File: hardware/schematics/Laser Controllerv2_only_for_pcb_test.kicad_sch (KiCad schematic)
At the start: 98 parts, among them J1 SD Card Module (6-pin, 2.54mm), J2 PWR IN VIN_BUCK (10-30V), J3 PWR IN Galvo, J4 FAN1 PWR IN, J5 FAN1, J6 FAN2 PWR IN, J7 FAN2, U1 ESP32-S3-N16R8-DevKit, U10 DS18B20, U12 OPA4134UA_2K5, U13 Galvo Input, U15 6N137, U16 6N137, U17 6N137, U2 DAC8562SDGST, U3 TTL_RGB Blue, U4 TTL_RGB Red, U5 TTL_RGB Green, U6 DS18B20, U7 DS18B20, U8 DS18B20, U9 DS18B20

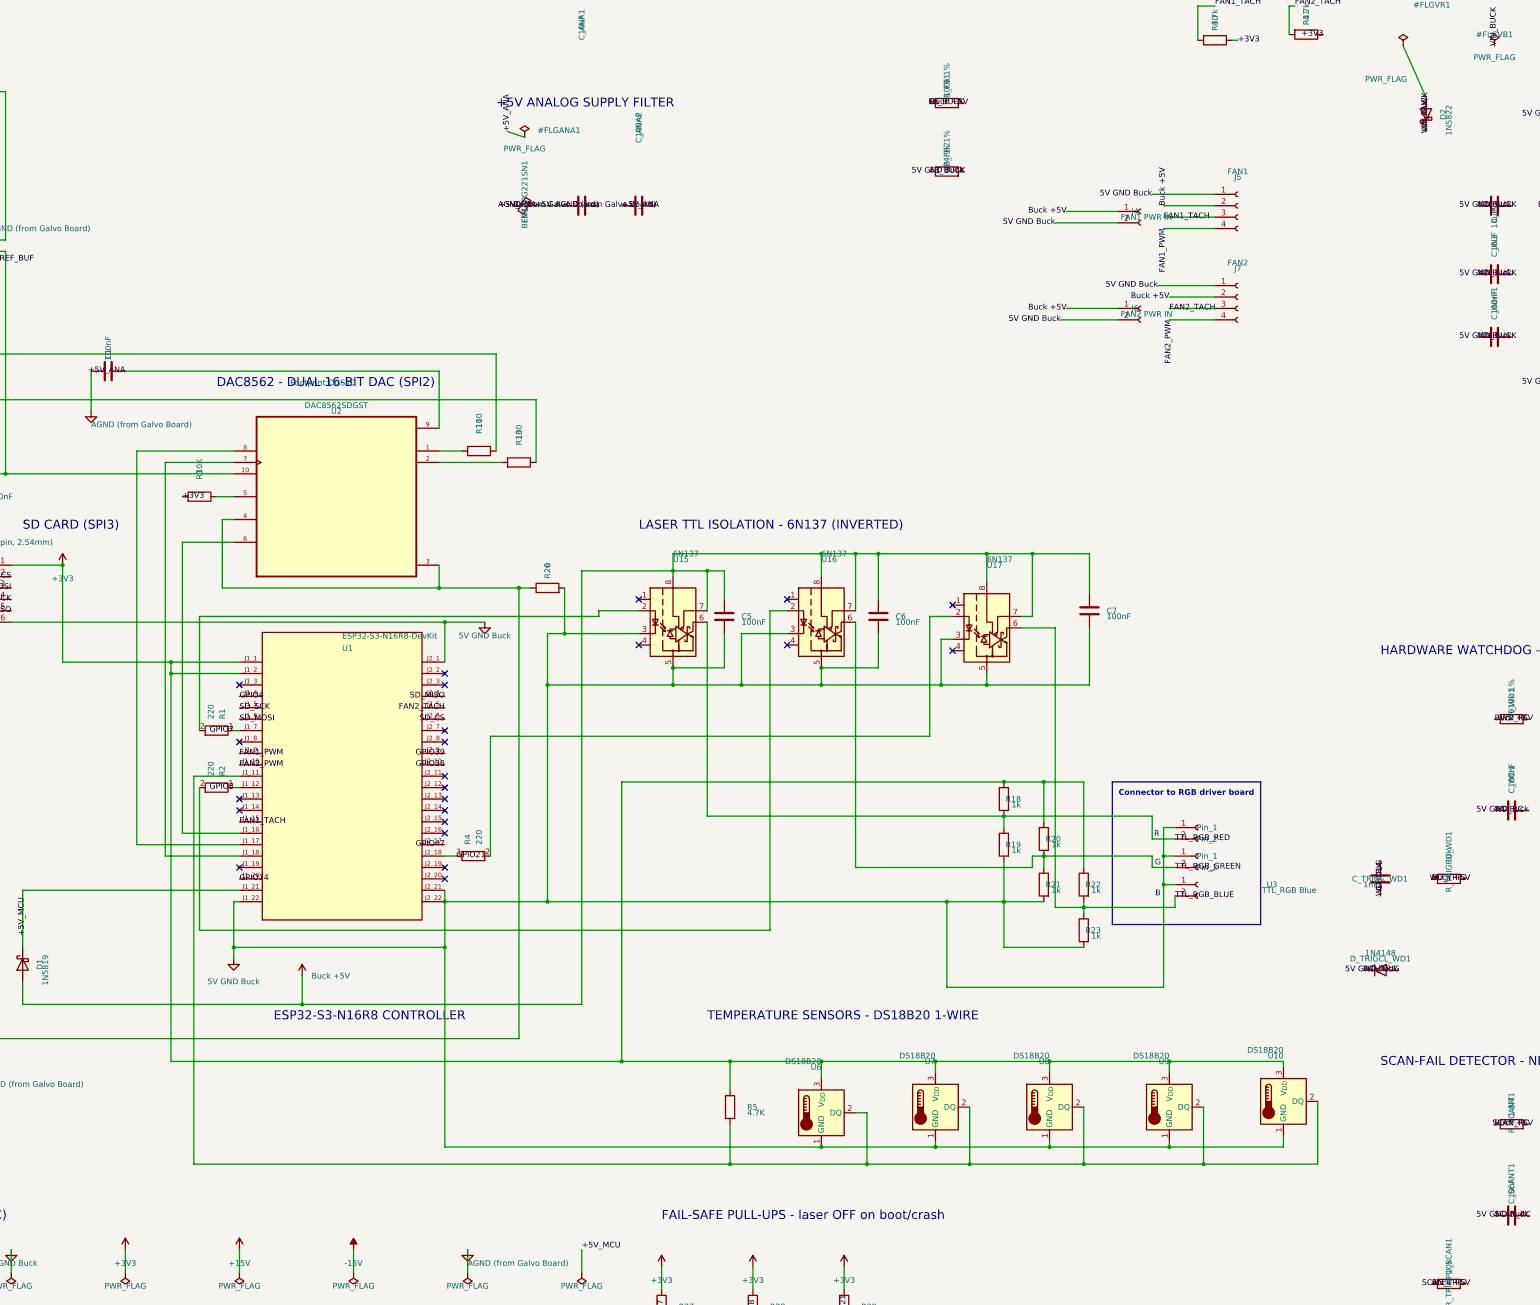
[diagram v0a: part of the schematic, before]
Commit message: hw: make v2 schematic portable and add supply decoupling
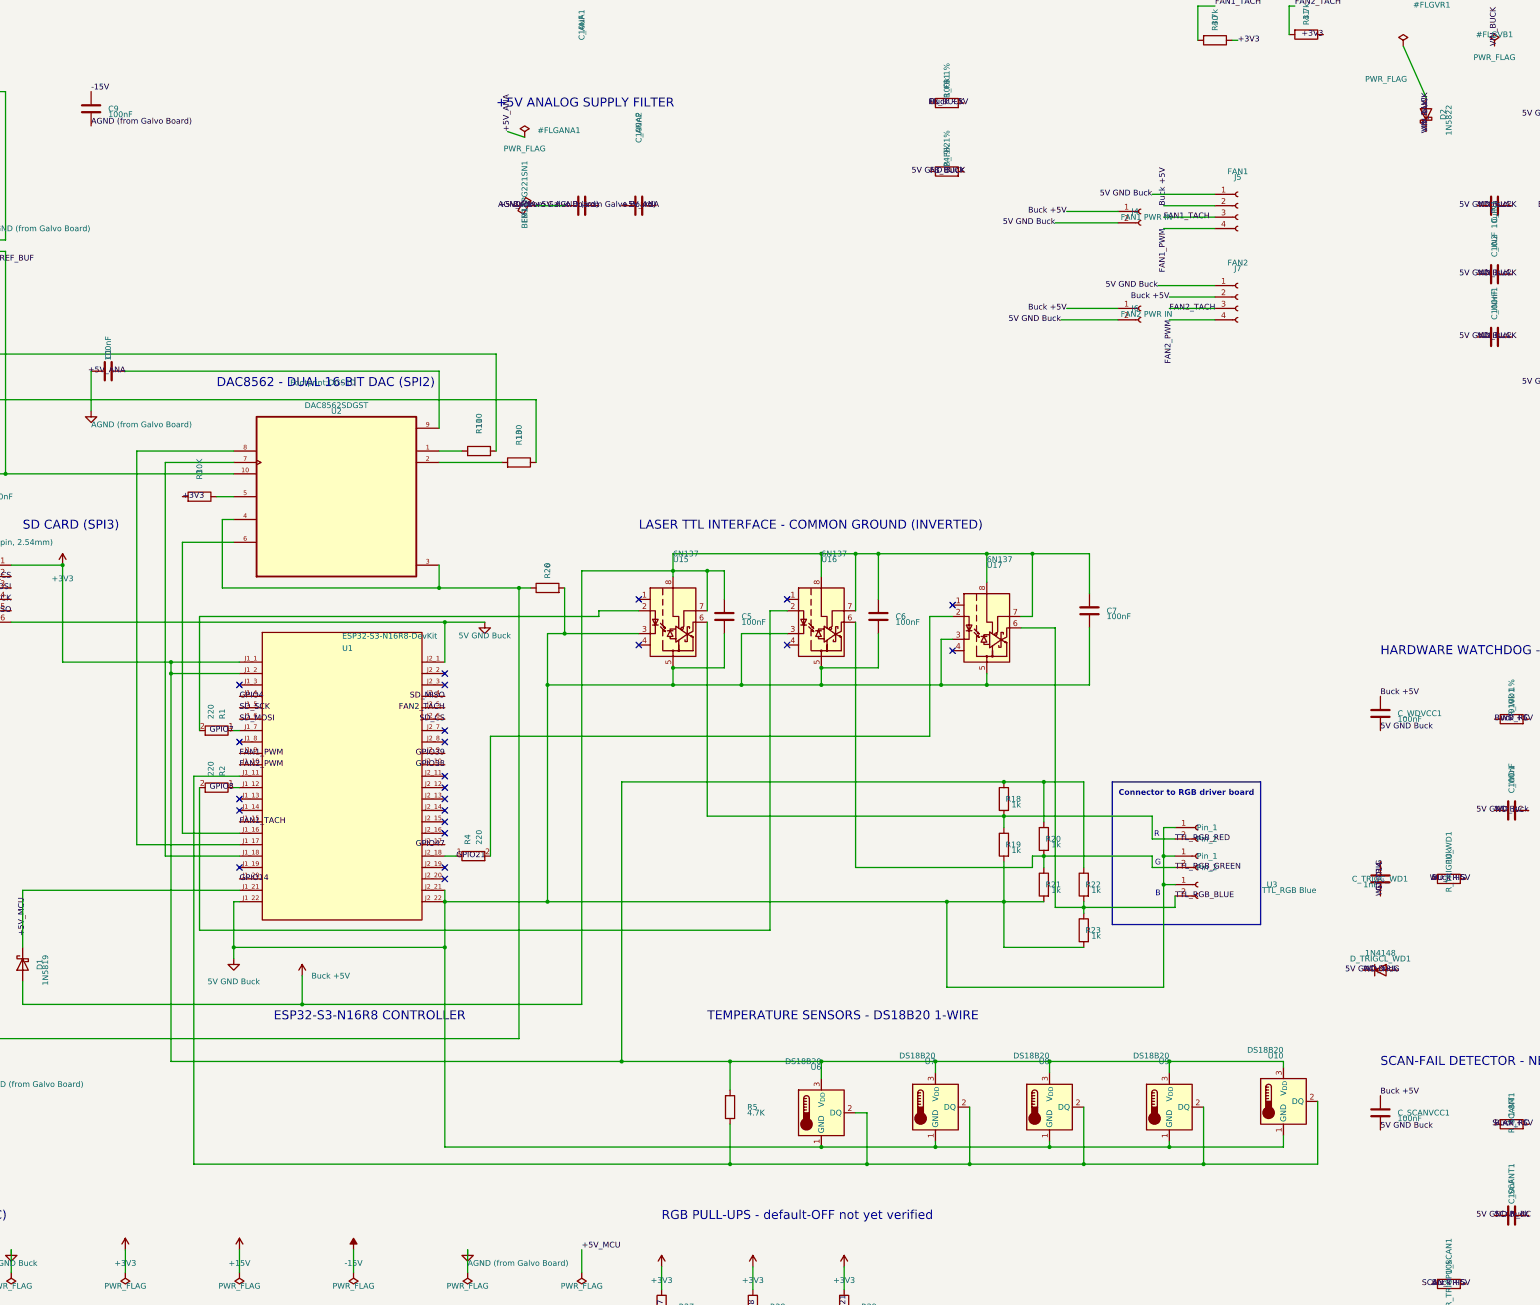
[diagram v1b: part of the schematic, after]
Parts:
- added C9, C_SCANVCC1, C_WDVCC1: 100nF, Capacitor_SMD:C_1206_3216Metric, symbol Device:C
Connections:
- net -15V: now also C9.1
- net 5V GND Buck: now also C_SCANVCC1.2, C_WDVCC1.2
- net AGND (from Galvo Board): now also C9.2
- net Buck +5V: now also C_SCANVCC1.1, C_WDVCC1.1
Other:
- note added: "LASER TTL INTERFACE - COMMON GROUND (INVERTED)"
- note added: "RGB PULL-UPS - default-OFF not yet verified"
- note removed: "FAIL-SAFE PULL-UPS - laser OFF on boot/crash"
- note removed: "LASER TTL ISOLATION - 6N137 (INVERTED)"
- title: GalvOS ESP32 Laser Controller Board V1.2.7 -> GalvOS ESP32 Laser Controller - V2 engineering review

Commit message: hw: add power-isolated DAC level translation and reset wiring
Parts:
- added C_DACLVA1, C_DACLVB1: 100nF, Capacitor_SMD:C_1206_3216Metric, symbol Device:C
- added R_DACCLR1, R_DACDIN1, R_DACSCLK1, R_DACSYNC1: 22, Resistor_SMD:R_1206_3216Metric, symbol Device:R
- added R_DACCLRA1, R_DACDINA1, R_DACDINB1, R_DACSCLKA1, R_DACSCLKB1, R_DACSYNCA1, R_DACSYNCB1, R_DACUNUSED1: 10k, Resistor_SMD:R_1206_3216Metric, symbol Device:R
- added U_DACLV1: SN74LVC8T245PWR, Package_SO:TSSOP-24_4.4x7.8mm_P0.65mm, symbol Logic_LevelTranslator:SN74LVC8T245
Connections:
- net +3V3: now also C_DACLVA1.1, R_DACCLRA1.1, R_DACSYNCA1.1, U_DACLV1.1 (V_{CCA}), U_DACLV1.2 (DIR); no longer R3.2
- net +5V_ANA: now also R3.2, C_DACLVB1.1, R_DACSYNCB1.1, U_DACLV1.23 (V_{CCB}), U_DACLV1.24 (V_{CCB})
- net AGND (from Galvo Board): now also C_DACLVA1.2, C_DACLVB1.2, R_DACDINA1.2, R_DACDINB1.2, R_DACSCLKA1.2, R_DACSCLKB1.2, R_DACUNUSED1.2, U_DACLV1.11 (GND), U_DACLV1.12 (GND), U_DACLV1.13 (GND), U_DACLV1.22 (~{OE})
- net DAC_CLR_5V: now reaches R3.1, U2.5 (CLR)
- net DAC_CLR_5V: now also R_DACCLR1.1
- net DAC_SYNC_3V3: now reaches U1.J1_16 (GPIO10)
- net DAC_SYNC_3V3: now also R_DACSYNCA1.2, U_DACLV1.5 (A3); no longer U2.6 (SYNC)
- net DAC_SCLK_3V3: now reaches U1.J1_18 (GPIO12)
- net DAC_SCLK_3V3: now also R_DACSCLKA1.1, U_DACLV1.3 (A1); no longer U2.7 (SCLK)
- net DAC_DIN_3V3: now reaches U1.J1_17 (GPIO11)
- net DAC_DIN_3V3: now also R_DACDINA1.1, U_DACLV1.4 (A2); no longer U2.8 (DIN)
- net DAC_CLR_3V3: now reaches U1.J1_19 (GPIO13)
- net DAC_CLR_3V3: now also R_DACCLRA1.2, U_DACLV1.6 (A4)
- new net: R_DACCLR1.2, U_DACLV1.18 (B4)
- new net: R_DACDIN1.2, U_DACLV1.20 (B2)
- new net: R_DACSYNC1.2, U_DACLV1.19 (B3)
- new net: R_DACSCLK1.2, U_DACLV1.21 (B1)
- new net DAC_DIN_5V: R_DACDIN1.1, R_DACDINB1.1, U2.8 (DIN)
- new net DAC_SCLK_5V: R_DACSCLK1.1, R_DACSCLKB1.1, U2.7 (SCLK)
- new net DAC_SYNC_5V: R_DACSYNC1.1, R_DACSYNCB1.2, U2.6 (SYNC)
- new net DAC_UNUSED: R_DACUNUSED1.1, U_DACLV1.10 (A8), U_DACLV1.7 (A5), U_DACLV1.8 (A6), U_DACLV1.9 (A7)
- no-connect marks 25 -> 28
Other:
- note added: "DAC INPUT DEFAULTS / 3V3"
- note added: "DAC OUTPUT DEFAULTS / 5V"
- moved on the sheet: R3

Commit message: hw: v2.0.1-draft correct sensor connectors and fan tach mapping
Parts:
- U10, U6, U7, U8, U9: value DS18B20 -> DS18B20 connector; symbol Sensor_Temperature:DS18B20 -> Connector_Generic:Conn_01x03
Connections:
- net FAN1_TACH: now also U1.J2_5 (GPIO2); no longer U1.J1_15 (GPIO9)
- net FAN2_TACH: now also U1.J1_15 (GPIO9); no longer U1.J2_5 (GPIO2)

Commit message: feat(hw): add v2.0.2 draft PCB and fan supplies
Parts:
- J2: value PWR IN VIN_BUCK (10-30V) -> 12.6V IN (BUCK)
- J4: value FAN1 PWR IN -> FAN1 12V IN
- J6: value FAN2 PWR IN -> FAN2 12V IN
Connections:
- net Buck +5V: no longer J4.1 (Pin_1), J5.2 (Pin_2), J6.1 (Pin_1), J7.2 (Pin_2)
- new net FAN1_12V: J4.1 (Pin_1), J5.2 (Pin_2)
- new net FAN2_12V: J6.1 (Pin_1), J7.2 (Pin_2)
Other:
- note added: "BUCK CONVERTER LMR33630 - 12.6V INPUT TO +5V"
- note removed: "BUCK CONVERTER LMR33630 - VIN 10-30V TO +5V"
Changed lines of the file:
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@@
 		(title "GalvOS ESP32 Laser Controller - V2 engineering review")
 		(date "2026-09-14")
-		(rev "V2.0.1 DRAFT - NOT FOR FABRICATION")
+		(rev "V2.0.2 DRAFT - NOT FOR FABRICATION")
 	)
 	(rectangle
@@
 		)
 	)
-	(label "Buck +5V"
+	(label "FAN2_12V"
 		(at 420.37 123.19 180)
 		(effects
@@
 		)
 	)
-	(label "Buck +5V"
+	(label "FAN1_12V"
 		(at 441.96 100.33 90)
 		(effects
@@
 		)
 	)
-	(label "Buck +5V"
+	(label "FAN1_12V"
 		(at 420.37 101.6 180)
 		(effects
@@
 		)
 	)
-	(label "Buck +5V"
+	(label "FAN2_12V"
 		(at 443.23 120.65 180)
 		(effects
@@
 			)
 		)
-		(property "Value" "PWR IN VIN_BUCK (10-30V)"
+		(property "Value" "12.6V IN (BUCK)"
 			(at 88.9 335.74 0)
 			(show_name no)
@@
 			)
 		)
-		(property "Description" "PSU raw input, 10-30V, to onboard buck via D2 reverse-polarity protection"
+		(property "Description" "External 12.6V input to onboard buck through D2; fan 12V inputs are separate"
 			(at 449.58 245.11 0)
 			(hide yes)
@@
 			)
 		)
-		(property "Value" "FAN2 PWR IN"
+		(property "Value" "FAN2 12V IN"
 			(at 438.15 124.46 0)
 			(show_name no)
@@
 			)
 		)
-		(property "Value" "FAN1 PWR IN"
+		(property "Value" "FAN1 12V IN"
 			(at 438.15 102.86999999999999 0)
 			(show_name no)
@@
 		)
 	)
-	(text "BUCK CONVERTER LMR33630 - VIN 10-30V TO +5V"
+	(text "BUCK CONVERTER LMR33630 - 12.6V INPUT TO +5V"
 		(exclude_from_sim no)
 		(at 355.6 20.32 0)
